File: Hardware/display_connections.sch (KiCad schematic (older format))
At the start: 7 parts

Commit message: Modified TQFP100 pcbnew lib & first version of QSOP16 pcbnew lib
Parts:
- gave numbers to parts that had none: 7
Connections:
- net labels added: +12V, +3.3V, CS, IM0, IM1, IM2, IM3, IOVCC, LED1+, LED2+, LED3+, LED4+, LEDGND, RD, RESET, RS, S65_Backlight, SPI1_MISO, SPI1_MOSI, SPI1_SCK, VCC, VCI, X+, X-, Y+, Y-
- wire segments 9 -> 81

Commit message: First test version with hardware for the new MI0283QT-2 LCD
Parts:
- removed D3: BAT54, symbol ZENER
- removed D4, D5: 6.2V, symbol DIODE
- removed L1: 820uH, symbol INDUCTOR
- removed P15: CONN_13X2, symbol CONN_13X2
- removed Q1: BSS123, symbol MOSFET_N
- removed R17: 470k, symbol R
- added P12: DISPLAY_CTRL, symbol CONN_10X2
- added P13: DISPLAY_LED, symbol CONN_2X2
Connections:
- net labels added: LED1PWM, LED2PWM, LED3PWM, LED4PWM
- net labels removed: +12V, +5V, LED1+, LED2+, LED3+, LED4+, S65_Backlight
- wire segments 81 -> 69

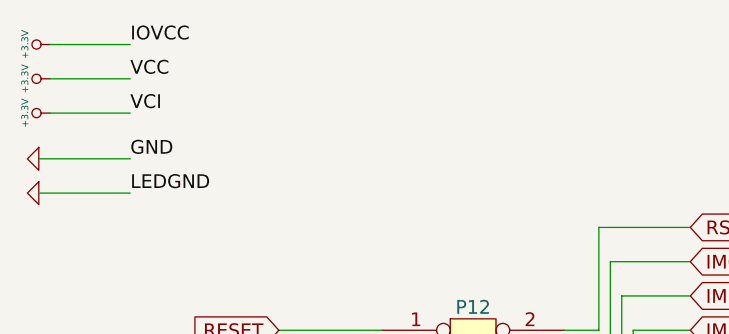
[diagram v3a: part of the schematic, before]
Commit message: updated display board, connection to mainboard updated
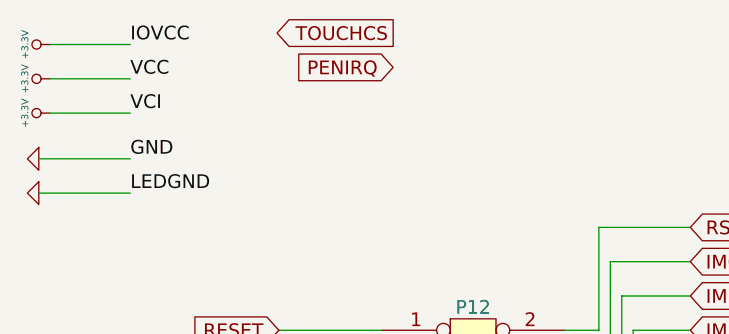
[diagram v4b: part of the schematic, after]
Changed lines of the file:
@@
-EESchema Schematic File Version 2  date Mi 01 Sep 2010 19:34:14 CEST
+EESchema Schematic File Version 2  date 14.09.2010 06:42:34
 LIBS:power
 LIBS:device
@@
 LIBS:STM32F10xVx
 LIBS:AD7843
+LIBS:LM75CIM
 LIBS:bordcomputer-cache
 EELAYER 24  0
@@
 Sheet 2 3
 Title ""
-Date "1 sep 2010"
+Date "14 sep 2010"
 Rev ""
 Comp ""
@@
 Comment4 ""
 $EndDescr
+Text GLabel 2400 2100 0    60   Output ~ 0
+TOUCHCS
+Text GLabel 2400 2250 0    60   Input ~ 0
+PENIRQ
 Wire Wire Line
 	1900 4550 2300 4550
